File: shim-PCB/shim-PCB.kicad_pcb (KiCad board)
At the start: 4 copper layers, 67.5 x 99.2 mm, 29 parts, among them J1 ROMI-Encoder, J10 LineSensor, J11 LineSensor, J12 SPI, J13 Ultrasonic., J14 THING, J15 THING, J16 ROMI, J17 i2c, J2 ROMI-Encoder, J3 Conn_01x19_Female, J4 ServoAnalog, J5 Conn_01x19_Female, J6 Conn_01x19_Female, J7 ROMI, J8 ROMI, J9 Conn_01x19_Female

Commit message: fix drc error
Resolves #40
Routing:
- net GPIO34: track 85.1 -> 86.3 mm
- net GPIO22: track 79.2 -> 80.1 mm
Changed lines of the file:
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@@
     (thickness 1.6)
     (drawings 161)
-    (tracks 521)
+    (tracks 526)
     (zones 0)
     (modules 29)
@@
     (1 In1.Cu signal)
     (2 In2.Cu signal)
-    (31 B.Cu signal hide)
+    (31 B.Cu signal)
     (32 B.Adhes user hide)
     (33 F.Adhes user hide)
@@
     (35 F.Paste user hide)
     (36 B.SilkS user hide)
-    (37 F.SilkS user)
+    (37 F.SilkS user hide)
     (38 B.Mask user hide)
-    (39 F.Mask user)
+    (39 F.Mask user hide)
     (40 Dwgs.User user hide)
     (41 Cmts.User user hide)
     (42 Eco1.User user hide)
     (43 Eco2.User user hide)
-    (44 Edge.Cuts user)
+    (44 Edge.Cuts user hide)
     (45 Margin user hide)
     (46 B.CrtYd user hide)
@@
       (drillshape 0)
       (scaleselection 1)
-      (outputdirectory "gerbers"))
+      (outputdirectory "gerbers-v2"))
   )
   (net 0 "")
@@
   (segment (start 129.8887 129.9074) (end 129.8887 129.54) (width 0.25) (layer In2.Cu) (net 14))
   (segment (start 120.904 114.554) (end 120.904 122.174) (width 0.25) (layer In2.Cu) (net 14) (status 30))
+  (segment (start 129.8887 129.54) (end 131.064 129.54) (width 0.25) (layer In2.Cu) (net 14))
   (segment (start 123.444 114.554) (end 123.444 122.174) (width 0.25) (layer In2.Cu) (net 15) (status 30))
   (segment (start 118.364 106.02) (end 118.364 104.8447) (width 0.25) (layer In2.Cu) (net 16) (status 10))
@@
   (segment (start 113.284 107.1953) (end 114.4593 108.3706) (width 0.25) (layer In1.Cu) (net 26))
   (segment (start 114.4593 108.3706) (end 114.4593 122.7228) (width 0.25) (layer In1.Cu) (net 26))
-  (segment (start 114.4593 122.7228) (end 126.4511 134.7146) (width 0.25) (layer In1.Cu) (net 26))
   (segment (start 126.4511 134.7146) (end 137.7626 134.7146) (width 0.25) (layer In1.Cu) (net 26))
   (segment (start 137.7626 134.7146) (end 140.208 137.16) (width 0.25) (layer In1.Cu) (net 26) (status 20))
@@
   (segment (start 113.284 92.7677) (end 115.824 90.2277) (width 0.25) (layer In2.Cu) (net 26))
   (segment (start 115.824 89.0524) (end 115.824 90.2277) (width 0.25) (layer In2.Cu) (net 26) (status 10))
+  (segment (start 118.3915 126.655) (end 119.797 126.655) (width 0.25) (layer In1.Cu) (net 26))
+  (segment (start 114.4593 122.7228) (end 118.3915 126.655) (width 0.25) (layer In1.Cu) (net 26))
+  (segment (start 120.70925 127.56725) (end 120.70925 128.97275) (width 0.25) (layer In1.Cu) (net 26))
+  (segment (start 119.797 126.655) (end 120.70925 127.56725) (width 0.25) (layer In1.Cu) (net 26))
+  (segment (start 120.70925 128.97275) (end 126.4511 134.7146) (width 0.25) (layer In1.Cu) (net 26))
   (segment (start 118.364 77.724) (end 118.364 78.8993) (width 0.25) (layer In2.Cu) (net 27) (status 10))
   (segment (start 118.364 78.8993) (end 117.1829 80.0804) (width 0.25) (layer In2.Cu) (net 27))

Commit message: Swapped 26/27
#39
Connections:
- D2 pad 1: GPIO27 -> GPIO26
- D4 pad 1: GPIO26 -> GPIO27
- J1 pad 2: GPIO27 -> GPIO26
- J1 pad 3: GPIO26 -> GPIO27
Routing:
- net GPIO27: track 96.4 -> 94.8 mm
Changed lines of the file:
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@@
     (thickness 1.6)
     (drawings 161)
-    (tracks 526)
+    (tracks 525)
     (zones 0)
     (modules 29)
@@
       (net 1 GND))
     (pad 2 thru_hole oval (at 0 2.54 180) (size 1.7 1.7) (drill 1) (layers *.Cu *.Mask)
-      (net 20 GPIO27))
-    (pad 3 thru_hole oval (at 0 5.08 180) (size 1.7 1.7) (drill 1) (layers *.Cu *.Mask)
       (net 19 GPIO26))
+    (pad 3 thru_hole oval (at 0 5.08 180) (size 1.7 1.7) (drill 1) (layers *.Cu *.Mask)
+      (net 20 GPIO27))
     (pad 4 thru_hole oval (at 0 7.62 180) (size 1.7 1.7) (drill 1) (layers *.Cu *.Mask)
       (net 6 "Net-(J1-Pad4)"))
@@
     )
     (pad 1 thru_hole rect (at 0 0 90) (size 1.6 1.6) (drill 0.8) (layers *.Cu *.Mask)
-      (net 19 GPIO26))
+      (net 20 GPIO27))
     (pad 2 thru_hole oval (at 7.62 0 90) (size 1.6 1.6) (drill 0.8) (layers *.Cu *.Mask)
       (net 1 GND))
@@
       (net 1 GND))
     (pad 1 thru_hole rect (at 0 0 90) (size 1.6 1.6) (drill 0.8) (layers *.Cu *.Mask)
-      (net 20 GPIO27))
+      (net 19 GPIO26))
     (model ${KISYS3DMOD}/Diode_THT.3dshapes/D_DO-35_SOD27_P7.62mm_Horizontal.wrl
       (at (xyz 0 0 0))
@@
   (segment (start 129.8887 129.9074) (end 129.8887 129.54) (width 0.25) (layer In2.Cu) (net 14))
   (segment (start 120.904 114.554) (end 120.904 122.174) (width 0.25) (layer In2.Cu) (net 14) (status 30))
-  (segment (start 129.8887 129.54) (end 131.064 129.54) (width 0.25) (layer In2.Cu) (net 14))
+  (segment (start 129.8887 129.54) (end 131.064 129.54) (width 0.25) (layer In2.Cu) (net 14) (status 20))
   (segment (start 123.444 114.554) (end 123.444 122.174) (width 0.25) (layer In2.Cu) (net 15) (status 30))
   (segment (start 118.364 106.02) (end 118.364 104.8447) (width 0.25) (layer In2.Cu) (net 16) (status 10))
@@
   (segment (start 137.414 89.4447) (end 137.414 88.1458) (width 0.25) (layer In1.Cu) (net 19))
   (segment (start 137.414 88.1458) (end 138.684 86.8758) (width 0.25) (layer In1.Cu) (net 19))
-  (segment (start 163.74 62.6544) (end 162.6146 61.529) (width 0.25) (layer In1.Cu) (net 19) (status 10))
-  (segment (start 162.6146 61.529) (end 160.2448 61.529) (width 0.25) (layer In1.Cu) (net 19))
-  (segment (start 160.2448 61.529) (end 147.574 74.1998) (width 0.25) (layer In1.Cu) (net 19))
   (segment (start 147.574 74.1998) (end 147.574 78.1424) (width 0.25) (layer In1.Cu) (net 19))
   (segment (start 147.574 78.1424) (end 141.1912 84.5252) (width 0.25) (layer In1.Cu) (net 19))
@@
   (segment (start 140.6672 84.5252) (end 139.8593 85.3331) (width 0.25) (layer In1.Cu) (net 19))
   (segment (start 139.8593 85.3331) (end 139.8593 85.7005) (width 0.25) (layer In1.Cu) (net 19))
-  (segment (start 163.74 62.6544) (end 172.7207 62.6544) (width 0.25) (layer In1.Cu) (net 19) (status 10))
-  (segment (start 172.7207 62.6544) (end 172.7387 62.6364) (width 0.25) (layer In1.Cu) (net 19))
   (segment (start 138.684 85.7005) (end 139.8593 85.7005) (width 0.25) (layer In1.Cu) (net 19) (status 10))
   (segment (start 133.604 122.174) (end 133.604 114.554) (width 0.25) (layer In2.Cu) (net 19) (status 30))
-  (segment (start 173.914 62.6364) (end 172.7387 62.6364) (width 0.25) (layer In1.Cu) (net 19) (status 10))
+  (segment (start 160.275 63.5794) (end 161.2 62.6544) (width 0.25) (layer In1.Cu) (net 19))
+  (segment (start 158.1944 63.5794) (end 160.275 63.5794) (width 0.25) (layer In1.Cu) (net 19))
+  (segment (start 158.1944 63.5794) (end 147.574 74.1998) (width 0.25) (layer In1.Cu) (net 19))
+  (segment (start 163.722 65.1764) (end 161.2 62.6544) (width 0.25) (layer In2.Cu) (net 19))
+  (segment (start 173.914 65.1764) (end 163.722 65.1764) (width 0.25) (layer In2.Cu) (net 19))
   (segment (start 126.5717 106.02) (end 141.0361 91.5556) (width 0.25) (layer In1.Cu) (net 20) (status 10))
   (segment (start 141.0361 91.5556) (end 148.0371 91.5556) (width 0.25) (layer In1.Cu) (net 20))
@@
   (segment (start 150.114 84.373) (end 155.194 79.293) (width 0.25) (layer In1.Cu) (net 20))
   (segment (start 155.194 79.293) (end 155.194 74.1264) (width 0.25) (layer In1.Cu) (net 20))
-  (segment (start 155.194 74.1264) (end 164.144 65.1764) (width 0.25) (layer In1.Cu) (net 20))
-  (segment (start 164.144 65.1764) (end 173.914 65.1764) (width 0.25) (layer In1.Cu) (net 20) (status 20))
-  (segment (start 162.3253 62.6544) (end 162.3253 63.3577) (width 0.25) (layer In1.Cu) (net 20))
-  (segment (start 162.3253 63.3577) (end 164.144 65.1764) (width 0.25) (layer In1.Cu) (net 20))
   (segment (start 126.5717 106.02) (end 127.1593 106.02) (width 0.25) (layer In1.Cu) (net 20) (status 10))
   (segment (start 125.984 106.02) (end 126.5717 106.02) (width 0.25) (layer In1.Cu) (net 20) (status 30))
@@
   (segment (start 127.1593 106.3874) (end 134.9687 114.1968) (width 0.25) (layer In1.Cu) (net 20))
   (segment (start 134.9687 114.1968) (end 134.9687 114.554) (width 0.25) (layer In1.Cu) (net 20))
-  (segment (start 161.2 62.6544) (end 162.3253 62.6544) (width 0.25) (layer In1.Cu) (net 20) (status 10))
+  (segment (start 163.758 62.6364) (end 163.74 62.6544) (width 0.25) (layer In1.Cu) (net 20))
+  (segment (start 173.914 62.6364) (end 163.758 62.6364) (width 0.25) (layer In1.Cu) (net 20))
+  (segment (start 162.88845 63.50595) (end 163.74 62.6544) (width 0.25) (layer In1.Cu) (net 20))
+  (segment (start 162.88845 66.43195) (end 162.88845 63.50595) (width 0.25) (layer In1.Cu) (net 20))
+  (segment (start 155.194 74.1264) (end 162.88845 66.43195) (width 0.25) (layer In1.Cu) (net 20))
   (segment (start 114.4757 63.7798) (end 110.8003 60.1044) (width 0.25) (layer In1.Cu) (net 21))
   (segment (start 117.2887 62.6544) (end 117.2887 63.3577) (width 0.25) (layer In1.Cu) (net 21))
@@
   (segment (start 113.284 77.724) (end 113.284 78.8993) (width 0.25) (layer In2.Cu) (net 25) (status 10))
   (via (at 162.57 122.174) (size 0.8) (drill 0.4) (layers F.Cu B.Cu) (net 25))
-  (segment (start 164.181 120.563) (end 162.57 122.174) (width 0.25) (layer F.Cu) (net 25))
-  (segment (start 164.181 120.2055) (end 164.181 120.563) (width 0.25) (layer F.Cu) (net 25))
+  (segment (start 164.181 120.563) (end 162.57 122.174) (width 0.25) (layer F.Cu) (net 25) (status 10))
+  (segment (start 164.181 120.2055) (end 164.181 120.563) (width 0.25) (layer F.Cu) (net 25) (status 30))
   (segment (start 115.824 77.724) (end 115.824 78.8993) (width 0.25) (layer In2.Cu) (net 26) (status 10))
   (segment (start 115.824 78.8993) (end 114.6486 80.0747) (width 0.25) (layer In2.Cu) (net 26))
@@
   (via (at 167.65 122.174) (size 0.8) (drill 0.4) (layers F.Cu B.Cu) (net 29))
   (segment (start 166.781 121.305) (end 167.65 122.174) (width 0.25) (layer F.Cu) (net 29))
-  (segment (start 166.781 120.2055) (end 166.781 121.305) (width 0.25) (layer F.Cu) (net 29))
+  (segment (start 166.781 120.2055) (end 166.781 121.305) (width 0.25) (layer F.Cu) (net 29) (status 10))
   (segment (start 129.8456 86.8758) (end 125.4272 86.8758) (width 0.25) (layer In1.Cu) (net 30))
   (segment (start 125.4272 86.8758) (end 124.6193 86.0679) (width 0.25) (layer In1.Cu) (net 30))
@@
   (segment (start 149.86 134.9375) (end 149.86 137.16) (width 0.25) (layer In1.Cu) (net 54) (status 20))
   (via (at 165.5445 122.301) (size 0.8) (drill 0.4) (layers F.Cu B.Cu) (net 54))
-  (segment (start 165.481 120.2055) (end 165.481 122.2375) (width 0.25) (layer F.Cu) (net 54))
+  (segment (start 165.481 120.2055) (end 165.481 122.2375) (width 0.25) (layer F.Cu) (net 54) (status 10))
   (segment (start 165.481 122.2375) (end 165.5445 122.301) (width 0.25) (layer F.Cu) (net 54))
   (segment (start 165.4175 122.174) (end 165.5445 122.301) (width 0.25) (layer B.Cu) (net 54))

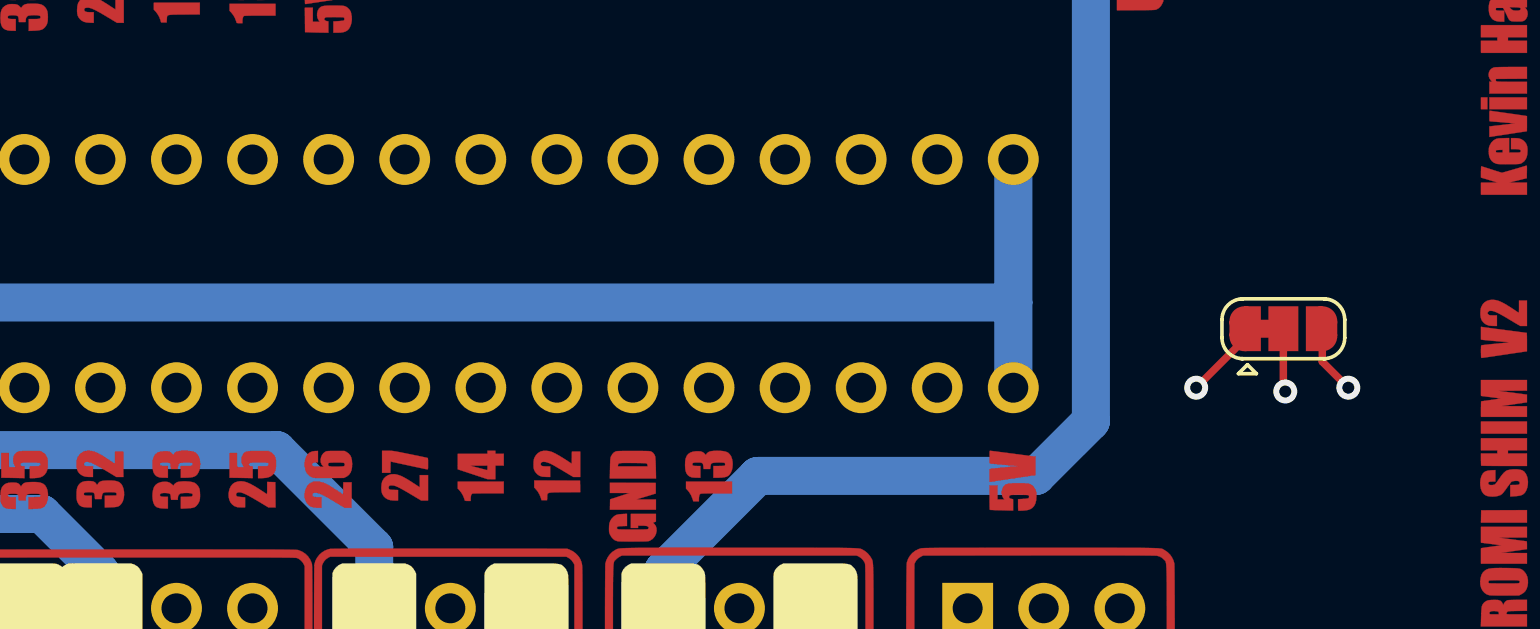
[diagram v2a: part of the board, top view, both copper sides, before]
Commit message: fixed drc error
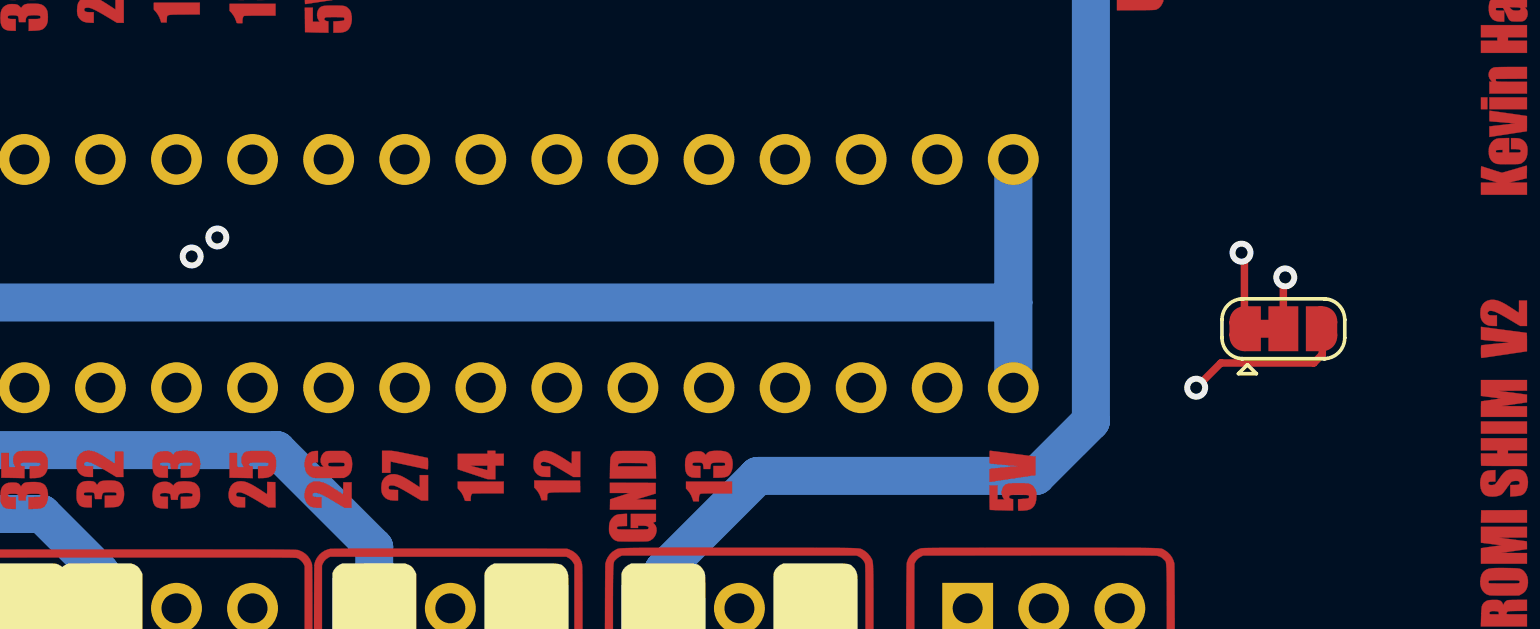
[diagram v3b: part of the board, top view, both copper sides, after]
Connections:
- J12 pad 2: SPI_DO -> GPIO23
- J17 pad 2: GPIO21 -> GPIO22
- J17 pad 3: GPIO22 -> SDA
- JP1 pad 1: GPIO23 -> GPIO21
- JP1 pad 2: SPI_DO -> SDA
- JP1 pad 3: GPIO21 -> GPIO23
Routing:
- net SDA: track 0.00 -> 64.5 mm, vias 0 -> 2
- net SPI_DO: track 28.8 -> 0.00 mm, vias 1 -> 0
- net GPIO23: track 96.7 -> 123.8 mm
- net GPIO21: track 121.8 -> 94.7 mm, vias 1 -> 2
- net GPIO22: track 80.1 -> 77.7 mm

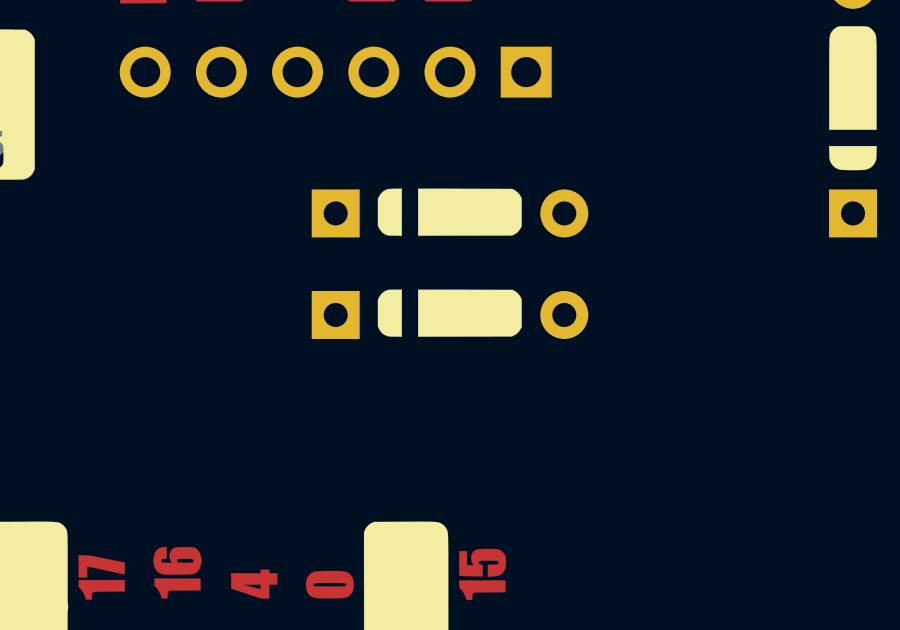
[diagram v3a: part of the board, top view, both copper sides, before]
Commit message: Removed zener on servo position pin. swapped labels
#42 closed  #43 closed
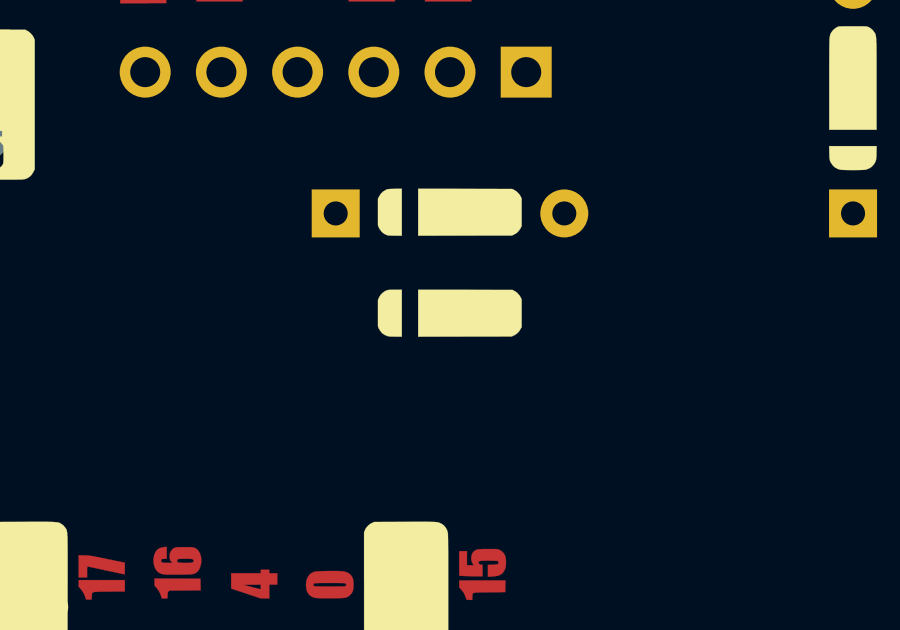
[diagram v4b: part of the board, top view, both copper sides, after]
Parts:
- removed D6: D_Zener, Diode_THT:D_DO-35_SOD27_P7.62mm_Horizontal
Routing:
- net GPIO34: track 86.3 -> 62.3 mm
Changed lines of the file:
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@@
     (thickness 1.6)
     (drawings 161)
-    (tracks 530)
+    (tracks 525)
     (zones 0)
-    (modules 29)
+    (modules 28)
     (nets 57)
   )
@@
     (35 F.Paste user hide)
     (36 B.SilkS user hide)
-    (37 F.SilkS user)
+    (37 F.SilkS user hide)
     (38 B.Mask user hide)
     (39 F.Mask user hide)
@@
   )
   (module Diode_THT:D_DO-35_SOD27_P7.62mm_Horizontal (layer F.Cu)
-    (at 143.955 66.04)
-    (descr "Diode, DO-35_SOD27 series, Axial, Horizontal, pin pitch=7.62mm, , length*diameter=4*2mm^2, , http://www.diodes.com/_files/packages/DO-35.pdf")
-    (tags "Diode DO-35_SOD27 series Axial Horizontal pin pitch 7.62mm  length 4mm diameter 2mm")
-    (fp_text reference D6 (at 3.81 -2.12) (layer F.SilkS) hide
-      (effects (font (size 1 1) (thickness 0.15)))
-    )
-    (fp_text value D_Zener (at 3.81 2.12) (layer F.Fab)
-      (effects (font (size 1 1) (thickness 0.15)))
-    )
-    (fp_line (start 0 0) (end 1.81 0) (layer F.Fab) (width 0.1))
-    (fp_line (start 7.62 0) (end 5.81 0) (layer F.Fab) (width 0.1))
-    (fp_line (start -1.05 -1.25) (end -1.05 1.25) (layer F.CrtYd) (width 0.05))
-    (fp_line (start -1.05 1.25) (end 8.67 1.25) (layer F.CrtYd) (width 0.05))
-    (fp_line (start 8.67 1.25) (end 8.67 -1.25) (layer F.CrtYd) (width 0.05))
-    (fp_line (start 8.67 -1.25) (end -1.05 -1.25) (layer F.CrtYd) (width 0.05))
-    (fp_text user K (at 0 -1.8) (layer F.Fab)
-      (effects (font (size 1 1) (thickness 0.15)))
-    )
-    (fp_text user K (at 0 -1.8) (layer F.SilkS) hide
-      (effects (font (size 1 1) (thickness 0.15)))
-    )
-    (pad 1 thru_hole rect (at 0 0) (size 1.6 1.6) (drill 0.8) (layers *.Cu *.Mask)
-      (net 14 GPIO34))
-    (pad 2 thru_hole oval (at 7.62 0) (size 1.6 1.6) (drill 0.8) (layers *.Cu *.Mask)
-      (net 1 GND))
-    (model ${KISYS3DMOD}/Diode_THT.3dshapes/D_DO-35_SOD27_P7.62mm_Horizontal.wrl
-      (at (xyz 0 0 0))
-      (scale (xyz 1 1 1))
-      (rotate (xyz 0 0 0))
-    )
-  )
-  (module Diode_THT:D_DO-35_SOD27_P7.62mm_Horizontal (layer F.Cu)
     (at 143.955 62.6544)
     (descr "Diode, DO-35_SOD27 series, Axial, Horizontal, pin pitch=7.62mm, , length*diameter=4*2mm^2, , http://www.diodes.com/_files/packages/DO-35.pdf")
@@
   (segment (start 134.7793 89.5396) (end 134.7793 88.0511) (width 0.25) (layer In1.Cu) (net 14))
   (segment (start 134.7793 88.0511) (end 133.604 86.8758) (width 0.25) (layer In1.Cu) (net 14))
-  (segment (start 133.604 85.7005) (end 133.604 84.5252) (width 0.25) (layer In1.Cu) (net 14) (status 10))
-  (segment (start 143.955 66.04) (end 143.955 68.1842) (width 0.25) (layer In1.Cu) (net 14) (status 10))
-  (segment (start 143.955 68.1842) (end 134.7793 77.3599) (width 0.25) (layer In1.Cu) (net 14))
-  (segment (start 134.7793 77.3599) (end 134.7793 83.3499) (width 0.25) (layer In1.Cu) (net 14))
-  (segment (start 134.7793 83.3499) (end 133.604 84.5252) (width 0.25) (layer In1.Cu) (net 14))
   (segment (start 120.904 122.174) (end 120.904 123.3493) (width 0.25) (layer In2.Cu) (net 14) (status 10))
   (segment (start 120.904 123.3493) (end 121.4916 123.3493) (width 0.25) (layer In2.Cu) (net 14))
@@
   (segment (start 119.797 126.655) (end 120.70925 127.56725) (width 0.25) (layer In1.Cu) (net 26))
   (segment (start 120.70925 128.97275) (end 126.4511 134.7146) (width 0.25) (layer In1.Cu) (net 26))
-  (segment (start 137.668 136.7777) (end 135.6049 134.7146) (width 0.25) (layer In1.Cu) (net 26))
-  (segment (start 137.668 137.16) (end 137.668 136.7777) (width 0.25) (layer In1.Cu) (net 26))
+  (segment (start 137.668 136.7777) (end 135.6049 134.7146) (width 0.25) (layer In1.Cu) (net 26) (status 10))
+  (segment (start 137.668 137.16) (end 137.668 136.7777) (width 0.25) (layer In1.Cu) (net 26) (status 30))
   (segment (start 126.4511 134.7146) (end 135.6049 134.7146) (width 0.25) (layer In1.Cu) (net 26))
   (segment (start 118.364 77.724) (end 118.364 78.8993) (width 0.25) (layer In2.Cu) (net 27) (status 10))
@@
   (segment (start 136.8425 133.223) (end 138.1125 133.223) (width 0.25) (layer In2.Cu) (net 56))
   (segment (start 133.223 129.6035) (end 136.8425 133.223) (width 0.25) (layer In2.Cu) (net 56))
-  (segment (start 140.208 135.3185) (end 140.208 137.16) (width 0.25) (layer In2.Cu) (net 56))
+  (segment (start 140.208 135.3185) (end 140.208 137.16) (width 0.25) (layer In2.Cu) (net 56) (status 20))
   (segment (start 138.1125 133.223) (end 140.208 135.3185) (width 0.25) (layer In2.Cu) (net 56))
   (zone (net 1) (net_name GND) (layer B.Cu) (hatch edge 0.508)
